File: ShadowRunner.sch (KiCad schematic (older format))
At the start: 70 parts

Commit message: Added RF Matching circuits
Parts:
- removed J?: Conn_Coaxial, symbol Connector:Conn_Coaxial
- removed R?: 0, symbol Device:R
- added C? (x4): NC, symbol Device:C
- added J?: MM8130-2600, symbol myPartsLibrary:MM8130-2600
- added J?: U.FL-R-SMT-1, symbol Connector:Conn_Coaxial
- added L?: NC, symbol pspice:INDUCTOR
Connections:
- net labels added: SWRESET
- net labels removed: RESET, SWO
- wire segments 291 -> 302
- no-connect marks 49 -> 50
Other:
- note removed: "ADD RF MATCHING AND COAX"
- note removed: "MM8130-2600"
- moved on the sheet: AE?, C?, L?, R?, U?

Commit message: Updated Schematic
-Added power supplies
-Added Battery
-Added 3 buttons
-Added 3 LEDs
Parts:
- removed C? (x4): C, symbol Device:C
- removed D? (x2): D, symbol Device:D
- removed D? (x2): D_Zener, symbol Device:D_Zener
- removed J?: Conn_01x20, symbol Connector_Generic:Conn_01x20
- removed L? (x2): L, symbol Device:L
- removed R? (x4): R, symbol Device:R
- removed R? (x2): 10K, symbol Device:R
- removed TP? (x2): TestPoint, symbol Connector:TestPoint
- removed U? (x2): LM2734Y, Package_TO_SOT_SMD:TSOT-23-6, symbol Regulator_Switching:LM2734Y
- added C? (x2): 10uF, symbol Device:C
- added C? (x2): 100uF, symbol Device:C
- added D? (x3): LED, symbol Device:LED
- added J?: micro JST SH, symbol Connector_Generic:Conn_01x02
- added Q? (x3): DMN65D8L, symbol Device:Q_NMOS_GDS
- added R?: 5.1K, symbol Device:R
- added R?: NC, symbol Device:R
- added R?: 220, symbol Device:R
- added R?: 360, symbol Device:R
- added R? (x5): 0, symbol Device:R
- added R?: 1000, symbol Device:R
- added R?: 440, symbol Device:R
- added R? (x6): 10K, symbol Device:R
- added R? (x3): 100, symbol Device:R
- added SW? (x3): SW_Push, symbol Switch:SW_Push
- added U?: USB-C, symbol myPartsLibrary:USB-C
- added U? (x2): LM1117-ADJ, symbol Regulator_Linear:LM1117-ADJ
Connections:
- net labels added: VBUS
- net labels removed: +3.3V, USB4085-GF-A(Digikey), V_BAT
- wire segments 302 -> 346
- no-connect marks 50 -> 56
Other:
- note added: "ASR00012"
- note added: "VERIFY FOOTPRINT!!"
- moved on the sheet: C?, J?, U?

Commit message: Creating netlist
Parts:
- AE1: renamed from AE?; value P822601 -> ACAG0301-1575-T
- gave numbers to parts that had none: 90

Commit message: Making footprints
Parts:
- removed Q1, Q2, Q3: DMN65D8L, symbol Device:Q_NMOS_GDS
- removed SW1, SW2, SW3: SW_Push, symbol Switch:SW_Push
- added Q1, Q2, Q3: DMN65D8L, Package_TO_SOT_SMD:SOT-23, symbol Device:Q_NMOS_GSD
- added U10, U8, U9: PTS645SM43SMTR92, MyLibs:PTS645SM43SMTR92, symbol myPartsLibrary:PTS645SM43SMTR92
- C1, C10, C11, C12, C13, C14, C15, C16, C17, C18, C19, C2, C20, C21, C22, C3, C4, C5, C6, C7, C8, C9: footprint (none) -> Capacitor_SMD:C_0402_1005Metric
- D1, D2, D3: footprint (none) -> LED_SMD:LED_0402_1005Metric
- J1: footprint (none) -> MyLibs:S2B-ZR-SM4A-TFLFSN
- J2: value Conn_02x05_Odd_Even -> GRPB052VWQS-RC; footprint (none) -> MyLibs:S2B-ZR-SM4A-TFLFSN
- R1, R10, R11, R12, R13, R14, R15, R16, R17, R18, R19, R2, R20, R21, R22, R23, R24, R25, R26, R27, R28, R29, R3, R30, R31, R32, R33, R34, R35, R36, R37, R38, R39, R4, R40, R5, R6, R7, R8, R9: footprint (none) -> Resistor_SMD:R_0402_1005Metric
- U1, U3: footprint (none) -> Package_TO_SOT_SMD:SOT-223
- U2: footprint (none) -> MyLibs:USB4085-GF-A
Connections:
- wire segments 346 -> 365
- no-connect marks 56 -> 78
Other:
- note added: "S2B-ZR-SM4A-TF(LF)(SN)"
- moved on the sheet: J2

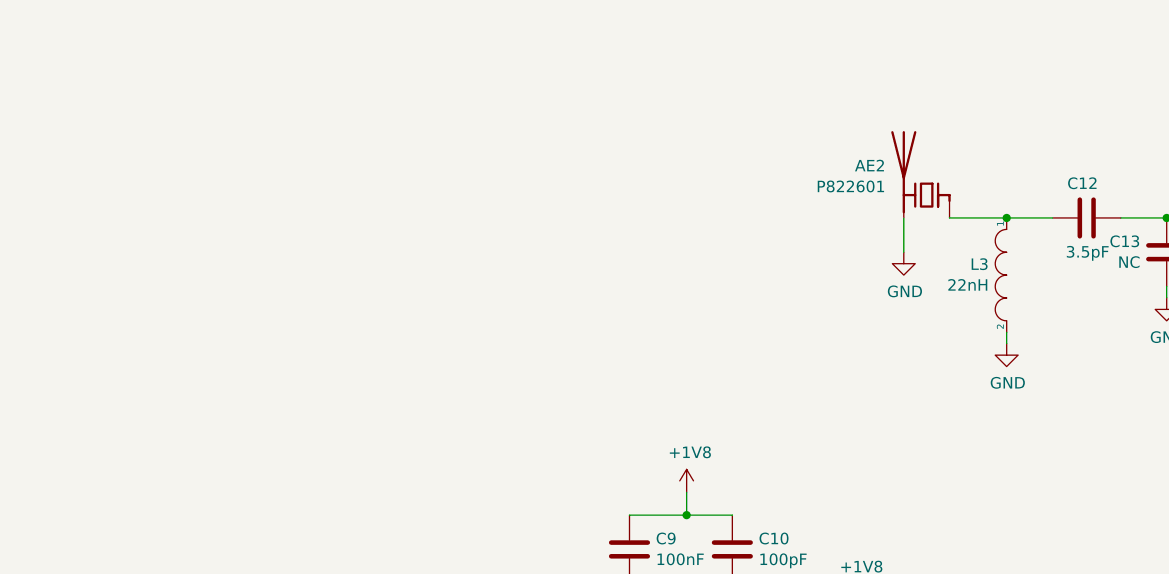
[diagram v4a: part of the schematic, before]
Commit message: Updating footprints.
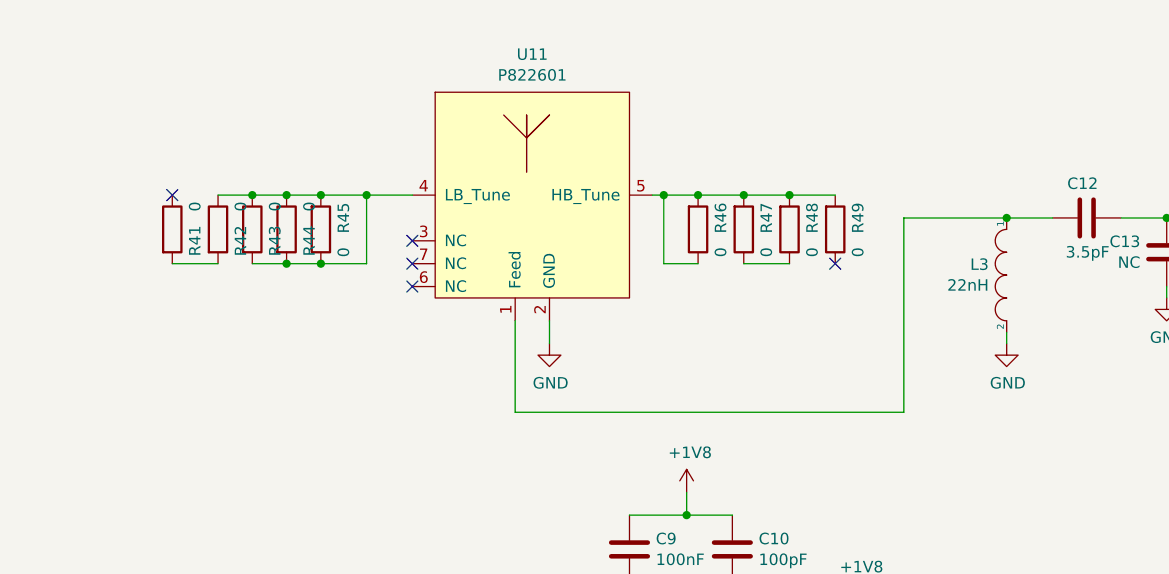
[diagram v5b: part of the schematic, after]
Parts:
- removed AE2: P822601, symbol Device:Antenna_Chip
- added R41, R42, R43, R44, R45, R46, R47, R48, R49: 0, Resistor_SMD:R_0402_1005Metric, symbol Device:R
- added U11: P822601, MyLibs:P822601, symbol myPartsLibrary:P822601
- AE1: footprint (none) -> MyLibs:ACAG0301-1575-T
- J3: footprint (none) -> MyLibs:26-KP13B-SF-PEJ(800)DKR-ND
- J4: footprint (none) -> MyLibs:MM8130-2600
- J5: footprint (none) -> MyLibs:U.FL-R-SMT-110
- L1, L2, L3, L4, L5, L6: footprint (none) -> Inductor_SMD:L_0402_1005Metric
- U4: footprint (none) -> Package_LGA:LGA-12_2x2mm_P0.5mm
- U5: footprint (none) -> MyLibs:SKY65943_11
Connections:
- net GND: now also U11.2 (GND)
- net at C12.1, L3.1: now also U11.1 (Feed)
- new net: R42.1, R43.1, R43.2, R44.1, R44.2, R45.1, R45.2, U11.4 (LB_Tune)
- new net: R46.1, R46.2, R47.2, R48.2, R49.2, U11.5 (HB_Tune)
- new net: R41.2, R42.2
- new net: R47.1, R48.1
- no-connect marks 78 -> 83
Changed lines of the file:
@@
 F 0 "L3" V 9604 1628 50  0000 L CNN
 F 1 "22nH" V 9695 1628 50  0000 L CNN
-F 2 "" H 9650 1550 50  0001 C CNN
+F 2 "Inductor_SMD:L_0402_1005Metric" H 9650 1550 50  0001 C CNN
 F 3 "~" H 9650 1550 50  0001 C CNN
 	1    9650 1550
@@
 F 0 "L4" H 11100 1119 50  0000 C CNN
 F 1 "1.5nH" H 11100 1210 50  0000 C CNN
-F 2 "" H 11100 1300 50  0001 C CNN
+F 2 "Inductor_SMD:L_0402_1005Metric" H 11100 1300 50  0001 C CNN
 F 3 "~" H 11100 1300 50  0001 C CNN
 	1    11100 1300
@@
 F 0 "AE1" H 5656 3327 50  0000 R CNN
 F 1 "ACAG0301-1575-T" H 5656 3236 50  0000 R CNN
-F 2 "" H 5700 3375 50  0001 C CNN
+F 2 "MyLibs:ACAG0301-1575-T" H 5700 3375 50  0001 C CNN
 F 3 "~" H 5700 3375 50  0001 C CNN
 	1    5800 3200
@@
 F 0 "L1" H 6450 3119 50  0000 C CNN
 F 1 "1.5nH" H 6450 3210 50  0000 C CNN
-F 2 "" H 6450 3300 50  0001 C CNN
+F 2 "Inductor_SMD:L_0402_1005Metric" H 6450 3300 50  0001 C CNN
 F 3 "~" H 6450 3300 50  0001 C CNN
 	1    6450 3300
@@
 F 0 "U5" H 8550 3950 50  0000 C CNN
 F 1 "SKY65943-11" H 9300 3950 50  0000 C CNN
-F 2 "" H 9000 3550 50  0001 C CNN
+F 2 "MyLibs:SKY65943_11" H 9000 3550 50  0001 C CNN
 F 3 "" H 9000 3550 50  0001 C CNN
 	1    9000 3550
@@
 F 0 "L2" H 9150 4450 50  0000 C CNN
 F 1 "9.1nH" H 8900 4450 50  0000 C CNN
-F 2 "" H 8950 4500 50  0001 C CNN
+F 2 "Inductor_SMD:L_0402_1005Metric" H 8950 4500 50  0001 C CNN
 F 3 "~" H 8950 4500 50  0001 C CNN
 	1    8950 4500
@@
 F 0 "L5" H 11650 2850 50  0000 C CNN
 F 1 "68nH" H 11400 2850 50  0000 C CNN
-F 2 "" H 11450 2900 50  0001 C CNN
+F 2 "Inductor_SMD:L_0402_1005Metric" H 11450 2900 50  0001 C CNN
 F 3 "~" H 11450 2900 50  0001 C CNN
 	1    11450 2900
@@
 F 0 "J3" H 8442 9725 50  0000 C CNN
 F 1 "SIM_Card" H 8442 9634 50  0000 C CNN
-F 2 "" H 8350 9550 50  0001 C CNN
+F 2 "MyLibs:26-KP13B-SF-PEJ(800)DKR-ND" H 8350 9550 50  0001 C CNN
 F 3 " ~" H 8300 9200 50  0001 C CNN
 	1    8350 9200
@@
 F 0 "J4" H 12100 1606 50  0000 C CNN
 F 1 "MM8130-2600" H 12100 1515 50  0000 C CNN
-F 2 "" H 12100 1300 50  0001 C CNN
+F 2 "MyLibs:MM8130-2600" H 12100 1300 50  0001 C CNN
 F 3 " ~" H 12100 1300 50  0001 C CNN
 	1    12100 1300
@@
 	-1   0    0    -1
 $EndComp
-$Comp
-L power:GND #PWR039
-U 1 1 5E87AD4B
-P 9200 1450
-F 0 "#PWR039" H 9200 1200 50  0001 C CNN
-F 1 "GND" H 9205 1277 50  0000 C CNN
-F 2 "" H 9200 1450 50  0001 C CNN
-F 3 "" H 9200 1450 50  0001 C CNN
-	1    9200 1450
-	1    0    0    -1
-$EndComp
-Wire Wire Line
-	9200 1450 9200 1300
-Wire Wire Line
-	9400 1300 9650 1300
 Wire Wire Line
 	9850 1300 9650 1300
@@
 F 0 "L6" H 12300 3500 50  0000 C CNN
 F 1 "NC" H 12050 3500 50  0000 C CNN
-F 2 "" H 12100 3550 50  0001 C CNN
+F 2 "Inductor_SMD:L_0402_1005Metric" H 12100 3550 50  0001 C CNN
 F 3 "~" H 12100 3550 50  0001 C CNN
 	1    12100 3550
@@
 F 0 "J5" H 12200 2775 50  0000 L CNN
 F 1 "U.FL-R-SMT-1" H 11850 2950 50  0000 L CNN
-F 2 "" H 12100 2800 50  0001 C CNN
+F 2 "MyLibs:U.FL-R-SMT-110" H 12100 2800 50  0001 C CNN
 F 3 " ~" H 12100 2800 50  0001 C CNN
 	1    12100 2800
@@
 F 0 "U4" H 4742 9915 50  0000 C CNN
 F 1 "LIS2DS12" H 4742 9824 50  0000 C CNN
-F 2 "" H 4850 9050 50  0001 C CNN
+F 2 "Package_LGA:LGA-12_2x2mm_P0.5mm" H 4850 9050 50  0001 C CNN
 F 3 "" H 4850 9050 50  0001 C CNN
 	1    4850 9050
@@
 Wire Wire Line
 	11400 7800 14300 7800
-$Comp
-L Device:Antenna_Chip AE2
-U 1 1 5E75CEF9
-P 9300 1200
-F 0 "AE2" H 9480 1327 50  0000 L CNN
-F 1 "P822601" H 9480 1236 50  0000 L CNN
-F 2 "" H 9200 1375 50  0001 C CNN
-F 3 "~" H 9200 1375 50  0001 C CNN
-	1    9300 1200
-	-1   0    0    -1
-$EndComp
 NoConn ~ 14300 4200
 NoConn ~ 14300 4300
@@
 	-1   0    0    -1
 $EndComp
+$Comp
+L myPartsLibrary:P822601 U11
+U 1 1 5F04989A
+P 7550 1200
+F 0 "U11" H 7575 1815 50  0000 C CNN
+F 1 "P822601" H 7575 1724 50  0000 C CNN
+F 2 "MyLibs:P822601" H 7550 1200 50  0001 C CNN
+F 3 "" H 7550 1200 50  0001 C CNN
+	1    7550 1200
+	1    0    0    -1
+$EndComp
+NoConn ~ 7050 1400
+NoConn ~ 7050 1500
+NoConn ~ 7050 1600
+$Comp
+L power:GND #PWR039
+U 1 1 5F0C3A91
+P 7650 1850
+F 0 "#PWR039" H 7650 1600 50  0001 C CNN
+F 1 "GND" H 7655 1677 50  0000 C CNN
+F 2 "" H 7650 1850 50  0001 C CNN
+F 3 "" H 7650 1850 50  0001 C CNN
+	1    7650 1850
+	1    0    0    -1
+$EndComp
+Wire Wire Line
+	7650 1750 7650 1850
+$Comp
+L Device:R R45
+U 1 1 5F0ED0D3
+P 6650 1350
+F 0 "R45" V 6750 1300 50  0000 C CNN
+F 1 "0" V 6750 1450 50  0000 C CNN
+F 2 "Resistor_SMD:R_0402_1005Metric" V 6580 1350 50  0001 C CNN
+F 3 "~" H 6650 1350 50  0001 C CNN
+	1    6650 1350
+	1    0    0    1
+$EndComp
+$Comp
+L Device:R R44
+U 1 1 5F0EDC4F
+P 6500 1350
+F 0 "R44" V 6600 1300 50  0000 C CNN
+F 1 "0" V 6600 1450 50  0000 C CNN
+F 2 "Resistor_SMD:R_0402_1005Metric" V 6430 1350 50  0001 C CNN
+F 3 "~" H 6500 1350 50  0001 C CNN
+	1    6500 1350
+	1    0    0    -1
+$EndComp
+$Comp
+L Device:R R43
+U 1 1 5F0EDE84
+P 6350 1350
+F 0 "R43" V 6450 1300 50  0000 C CNN
+F 1 "0" V 6450 1450 50  0000 C CNN
+F 2 "Resistor_SMD:R_0402_1005Metric" V 6280 1350 50  0001 C CNN
+F 3 "~" H 6350 1350 50  0001 C CNN
+	1    6350 1350
+	1    0    0    -1
+$EndComp
+$Comp
+L Device:R R42
+U 1 1 5F0EE0BF
+P 6200 1350
+F 0 "R42" V 6300 1300 50  0000 C CNN
+F 1 "0" V 6300 1450 50  0000 C CNN
+F 2 "Resistor_SMD:R_0402_1005Metric" V 6130 1350 50  0001 C CNN
+F 3 "~" H 6200 1350 50  0001 C CNN
+	1    6200 1350
+	1    0    0    -1
+$EndComp
+$Comp
+L Device:R R41
+U 1 1 5F0EE309
+P 6000 1350
+F 0 "R41" V 6100 1300 50  0000 C CNN
+F 1 "0" V 6100 1450 50  0000 C CNN
+F 2 "Resistor_SMD:R_0402_1005Metric" V 5930 1350 50  0001 C CNN
+F 3 "~" H 6000 1350 50  0001 C CNN
+	1    6000 1350
+	1    0    0    -1
+$EndComp
+Wire Wire Line
+	6350 1500 6500 1500
+Wire Wire Line
+	6500 1500 6650 1500
+Connection ~ 6500 1500
+Wire Wire Line
+	6200 1200 6350 1200
+Wire Wire Line
+	6350 1200 6500 1200
+Connection ~ 6350 1200
+Wire Wire Line
+	6650 1200 6850 1200
+Wire Wire Line
+	6650 1200 6500 1200
+Connection ~ 6650 1200
+Connection ~ 6500 1200
+Wire Wire Line
+	6200 1500 6000 1500
+NoConn ~ 6000 1200
+Wire Wire Line
+	6850 1200 6850 1500
+Wire Wire Line
+	6850 1500 6650 1500
+Connection ~ 6850 1200
+Wire Wire Line
+	6850 1200 7050 1200
+Connection ~ 6650 1500
+$Comp
+L Device:R R46
+U 1 1 5F370BD5
+P 8300 1350
+F 0 "R46" V 8400 1300 50  0000 C CNN
+F 1 "0" V 8400 1450 50  0000 C CNN
+F 2 "Resistor_SMD:R_0402_1005Metric" V 8230 1350 50  0001 C CNN
+F 3 "~" H 8300 1350 50  0001 C CNN
+	1    8300 1350
+	1    0    0    1
+$EndComp
+Wire Wire Line
+	8100 1200 8150 1200
+Wire Wire Line
+	8300 1500 8150 1500
+Wire Wire Line
+	8150 1500 8150 1200
+Connection ~ 8150 1200
+Wire Wire Line
+	8150 1200 8300 1200
+$Comp
+L Device:R R47
+U 1 1 5F3C966E
+P 8500 1350
+F 0 "R47" V 8600 1300 50  0000 C CNN
+F 1 "0" V 8600 1450 50  0000 C CNN
+F 2 "Resistor_SMD:R_0402_1005Metric" V 8430 1350 50  0001 C CNN
+F 3 "~" H 8500 1350 50  0001 C CNN
+	1    8500 1350
+	1    0    0    1
+$EndComp
+Wire Wire Line
+	8500 1200 8300 1200
+Connection ~ 8300 1200
+$Comp
+L Device:R R48
+U 1 1 5F3F672A
+P 8700 1350
+F 0 "R48" V 8800 1300 50  0000 C CNN
+F 1 "0" V 8800 1450 50  0000 C CNN
+F 2 "Resistor_SMD:R_0402_1005Metric" V 8630 1350 50  0001 C CNN
+F 3 "~" H 8700 1350 50  0001 C CNN
+	1    8700 1350
+	1    0    0    1
+$EndComp
+Wire Wire Line
+	8700 1200 8500 1200
+Connection ~ 8500 1200
+Wire Wire Line
+	8500 1500 8700 1500
+$Comp
+L Device:R R49
+U 1 1 5F451209
+P 8900 1350
+F 0 "R49" V 9000 1300 50  0000 C CNN
+F 1 "0" V 9000 1450 50  0000 C CNN
+F 2 "Resistor_SMD:R_0402_1005Metric" V 8830 1350 50  0001 C CNN
+F 3 "~" H 8900 1350 50  0001 C CNN
+	1    8900 1350
+	1    0    0    1
+$EndComp
+Wire Wire Line
+	8900 1200 8700 1200
+Connection ~ 8700 1200
+NoConn ~ 8900 1500
+Wire Wire Line
+	7500 1750 7500 2150
+Wire Wire Line
+	7500 2150 9200 2150
+Wire Wire Line
+	9200 2150 9200 1300
+Wire Wire Line
+	9200 1300 9650 1300
 $EndSCHEMATC

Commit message: Created footprints, generated netlist
Created footprints
Generated netlist
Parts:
- U6: footprint (none) -> MyLibs:CM1402
- U7: footprint (none) -> MyLibs:nRF9160
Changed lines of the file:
@@
 F 0 "U6" H 10200 9915 50  0000 C CNN
 F 1 "CM1402" H 10200 9824 50  0000 C CNN
-F 2 "" H 10200 9350 50  0001 C CNN
+F 2 "MyLibs:CM1402" H 10200 9350 50  0001 C CNN
 F 3 "" H 10200 9350 50  0001 C CNN
 	1    10150 9250
@@
 F 0 "U7" H 15200 7815 50  0000 C CNN
 F 1 "nRF9160" H 15200 7724 50  0000 C CNN
-F 2 "" H 14500 7700 50  0001 C CNN
+F 2 "MyLibs:nRF9160" H 14500 7700 50  0001 C CNN
 F 3 "" H 14500 7700 50  0001 C CNN
 	1    13650 4700

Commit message: Working on footprint.
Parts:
- removed D3: LED, LED_SMD:LED_0402_1005Metric, symbol Device:LED
- removed Q3: DMN65D8L, Package_TO_SOT_SMD:SOT-23, symbol Device:Q_NMOS_GSD
- removed R14, R23, R24: 10K, Resistor_SMD:R_0402_1005Metric, symbol Device:R
- removed R17: 100, Resistor_SMD:R_0402_1005Metric, symbol Device:R
- removed R18, R20, R21, R26, R27, R28, R29, R30, R31, R32, R33, R34, R35, R36, R37, R38, R39, R40, R41, R42, R43, R44, R45, R46, R47, R48, R49: 0, Resistor_SMD:R_0402_1005Metric, symbol Device:R
- removed U10: PTS645SM43SMTR92, MyLibs:PTS645SM43SMTR92, symbol myPartsLibrary:PTS645SM43SMTR92
- removed U11: P822601, MyLibs:P822601, symbol myPartsLibrary:P822601
- added AE2: Antenna_Chip, MyLibs:PCS.06.A, symbol Device:Antenna_Chip
- added D4: LED, LED_SMD:LED_0402_1005Metric, symbol Device:LED
- added D5: DIODE, Diode_SMD:D_0402_1005Metric, symbol pspice:DIODE
- added H1, H2, H3: MountingHole, MountingHole:MountingHole_2.5mm, symbol Mechanical:MountingHole
- added R50: 330, Resistor_SMD:R_0402_1005Metric, symbol Device:R
- J2: footprint MyLibs:S2B-ZR-SM4A-TFLFSN -> Connector_PinHeader_1.27mm:PinHeader_2x05_P1.27mm_Vertical_SMD
- R11: value 0 -> 10K
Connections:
- net +1V8: now also R11.1; no longer C10.1, C9.1
- net +3V3: no longer R11.1
- net ACC_CLK: now also U7.24 (P0.14/AIN1)
- net ACC_CS: now also U7.23 (P0.13/AIN0)
- net ACC_INT1: now also U7.28 (P0.17/AIN4)
- net ACC_INT2: now also U7.29 (P0.18/AIN5)
- net ACC_MISO: now also U7.26 (P0.16/AIN3)
- net ACC_MOSI: now also U7.25 (P0.15/AIN2)
- net GND: now also J3.GND1 (GND), J3.GND2 (GND), J3.GND3 (GND), J3.GND4 (GND), J3.GND5 (GND), J3.GND6 (GND), J4.GND1 (GND), J4.GND2, J4.GND3, J4.GND4, AE2.2 (PCB_Trace), D4.1 (K)
- net GPS_EN: now also U5.2 (VEN), U7.83 (P0.26)
- net SIM_1V8: now also U7.49 (SIM_1V8)
- net SIM_CLK: now also U7.46 (SIM_CLK)
- net SIM_DATA: now also U7.48 (SIM_IO)
- net SIM_DETECT: now also U7.45 (SIM_DET)
- net SIM_RST: now also U7.43 (SIM_RST)
- net SWDCLK: now also U7.33 (SWDCLK)
- net SWDIO: now also U7.34 (SWDIO)
- net SWRESET: now also U7.32 (nRESET)
- net VBUS: now also D5.2 (A); no longer U2.A4, U2.A9, U2.B4, U2.B9
- net at C12.1, L3.1: now also AE2.1 (FEED)
- net at C17.1, L4.2: now also J4.SIG1 (In)
- net at C8.2, L1.1: now also U5.5 (RF_IN)
- net at U5.10 (RF_OUT): now also C15.2
- net at J4.SIG2 (Out): now also U7.61 (ANT)
- net at U7.88 (P0.30), U9.1, U9.2: now also R11.2
- new net: C10.1, C9.1
- new net: D5.1 (K), R50.1, U2.A4, U2.A9, U2.B4, U2.B9
- new net: D4.2 (A), R50.2
- no-connect marks 83 -> 79
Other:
- moved on the sheet: J4, R5, R6, U2

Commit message: Layout improved.
Let's see if I'll be able to route this thing....
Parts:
- removed H1, H2, H3: MountingHole, MountingHole:MountingHole_2.5mm, symbol Mechanical:MountingHole
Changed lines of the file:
@@
 Wire Wire Line
 	6850 3300 8400 3300
-$Comp
-L Mechanical:MountingHole H1
-U 1 1 5FFF17A9
-P 10650 10200
-F 0 "H1" H 10750 10246 50  0000 L CNN
-F 1 "MountingHole" H 10450 10100 50  0000 L CNN
-F 2 "MountingHole:MountingHole_2.5mm" H 10650 10200 50  0001 C CNN
-F 3 "~" H 10650 10200 50  0001 C CNN
-	1    10650 10200
-	1    0    0    -1
-$EndComp
-$Comp
-L Mechanical:MountingHole H2
-U 1 1 5FFF1E5E
-P 11250 10200
-F 0 "H2" H 11350 10246 50  0000 L CNN
-F 1 "MountingHole" H 11000 10100 50  0000 L CNN
-F 2 "MountingHole:MountingHole_2.5mm" H 11250 10200 50  0001 C CNN
-F 3 "~" H 11250 10200 50  0001 C CNN
-	1    11250 10200
-	1    0    0    -1
-$EndComp
-$Comp
-L Mechanical:MountingHole H3
-U 1 1 5FFF22E7
-P 11750 10200
-F 0 "H3" H 11850 10246 50  0000 L CNN
-F 1 "MountingHole" H 11650 10100 50  0000 L CNN
-F 2 "MountingHole:MountingHole_2.5mm" H 11750 10200 50  0001 C CNN
-F 3 "~" H 11750 10200 50  0001 C CNN
-	1    11750 10200
-	1    0    0    -1
-$EndComp
 Wire Wire Line
 	14000 3550 14300 3550
